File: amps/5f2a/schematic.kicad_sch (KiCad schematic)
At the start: 31 parts, among them T2 SE 5k:8

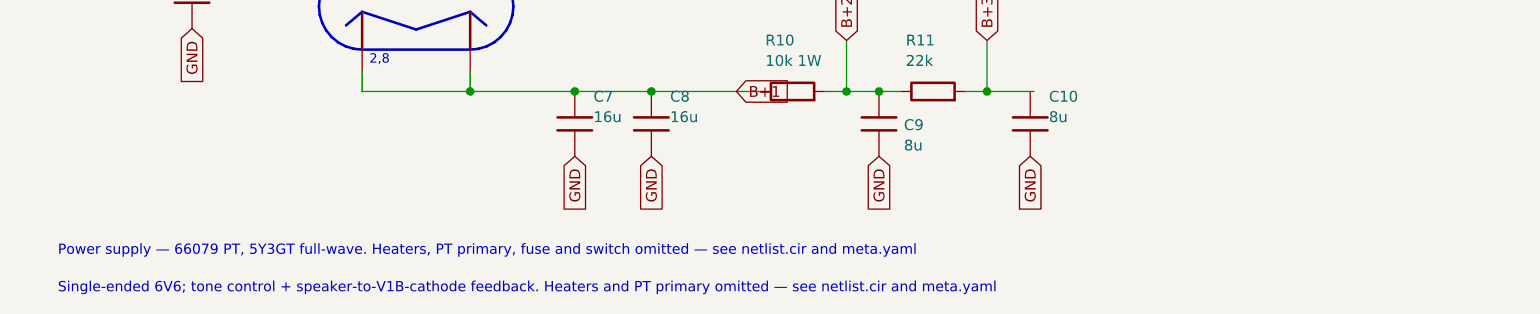
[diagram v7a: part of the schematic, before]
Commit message: Fix: schematic sheet notes no longer name repository files
Thirty-seven committed sheets rendered footnotes and section notes such as
"Heaters and PT primary omitted — see netlist.cir and meta.yaml" or
"excluded from netlist.cir (notes.md)" to visitors through KiCanvas. The
prose sweeps never counted sheets. Rewritten in the site's own words — the
netlist, the sources list, the circuit story, the parts list, the board
drawing — in 59 strings across 33 draw scripts, keeping every technical
claim as it was; the three tone sheets (6G4, 6G5, 6G6-B) are under repair
elsewhere and keep theirs for now. The sweep touched only strings passed to
the sheet's note, text, caption and footnote calls, never a path or a value.

Gates: check_schematics 40/0, connectivity 0 isolated pins;
verify_schematic_nets 40 clean; only the regenerated sheets and their served
copies changed.

Co-Authored-By: Claude Fable 5.1 <noreply@anthropic.com>
Claude-Session: https://claude.ai/code/session_01KBMfdh37HmCL2iWcBiL5J1
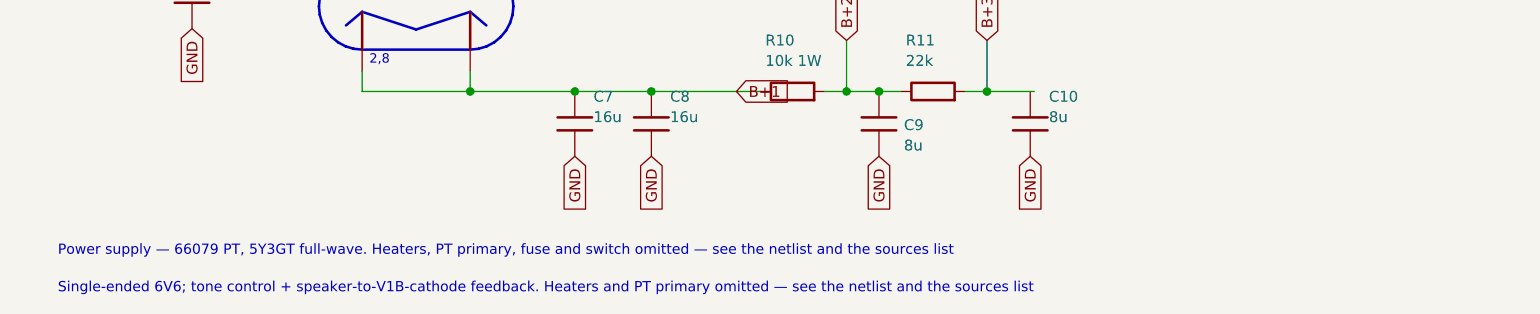
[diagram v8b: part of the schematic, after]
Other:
- note added: "Power supply — 66079 PT, 5Y3GT full-wave. Heaters, PT primary, fuse and switch omitted — see the netlist and the sources list"
- note added: "Single-ended 6V6; tone control + speaker-to-V1B-cathode feedback. Heaters and PT primary omitted — see the netlist and the sources list"
- note removed: "Power supply — 66079 PT, 5Y3GT full-wave. Heaters, PT primary, fuse and switch omitted — see netlist.cir and meta.yaml"
- note removed: "Single-ended 6V6; tone control + speaker-to-V1B-cathode feedback. Heaters and PT primary omitted — see netlist.cir and meta.yaml"
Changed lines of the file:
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@@
   (text "4" (at 62.0224 95.928 0)
     (effects (font (size 1.1 1.1)) (justify left)))
-  (text "Power supply — 66079 PT, 5Y3GT full-wave. Heaters, PT primary, fuse and switch omitted — see netlist.cir and meta.yaml" (at 12.7 131.056 0)
+  (text "Power supply — 66079 PT, 5Y3GT full-wave. Heaters, PT primary, fuse and switch omitted — see the netlist and the sources list" (at 12.7 131.056 0)
     (effects (font (size 1.2 1.2)) (justify left)))
-  (text "Single-ended 6V6; tone control + speaker-to-V1B-cathode feedback. Heaters and PT primary omitted — see netlist.cir and meta.yaml" (at 12.7 135.456 0)
+  (text "Single-ended 6V6; tone control + speaker-to-V1B-cathode feedback. Heaters and PT primary omitted — see the netlist and the sources list" (at 12.7 135.456 0)
     (effects (font (size 1.2 1.2)) (justify left)))
   (sheet_instances (path "/" (page "1")))
